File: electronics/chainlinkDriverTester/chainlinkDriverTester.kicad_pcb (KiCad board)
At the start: 2 copper layers, 198.1 x 95.2 mm, 151 parts, among them J1 Barrel_Jack_Switch, J10 Sensor C, J11 Sensor D, J12 Motor E, J13 Motor F, J14 Sensor E, J15 Sensor F, J2 Conn_01x03_Female, J22 Power, J26 exp, J27 exp, J28 exp, J29 exp, J3 Motor A, J30 exp, J31 exp, J32 Conn_01x06_Female, J5 Motor B, J6 Motor C, J7 Motor D, J8 Sensor A, J9 Sensor B, U1 AP7361C-33E, U2 TTGO_TDisplay, U3 VN7007ALH, U4 MCP23017_SS, U5 INA219BxD, U6 SN74LV1T34DBV, U7 Buck

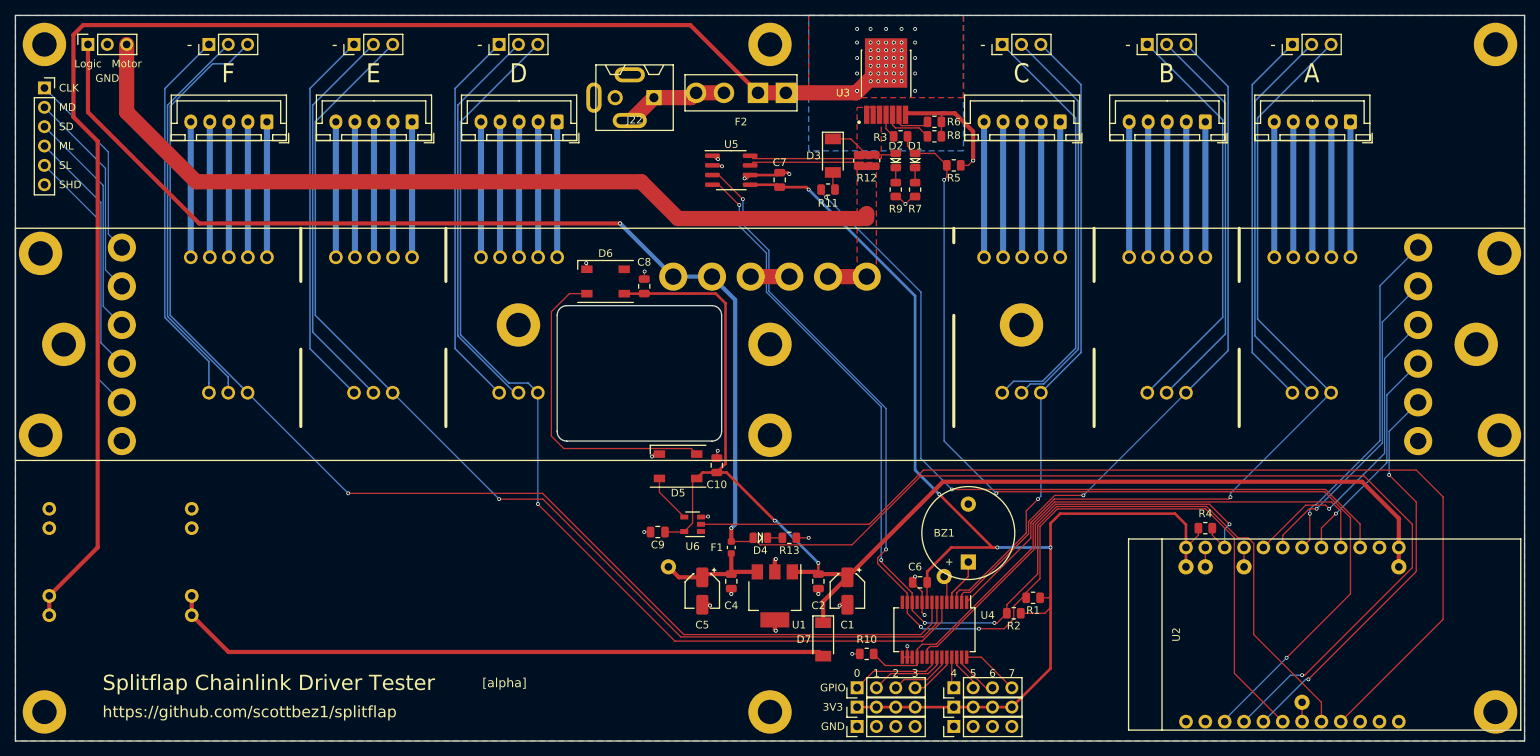
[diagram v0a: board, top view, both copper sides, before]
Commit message: chainlinkDriverTester: remove WS2812B LEDs, add detection switch
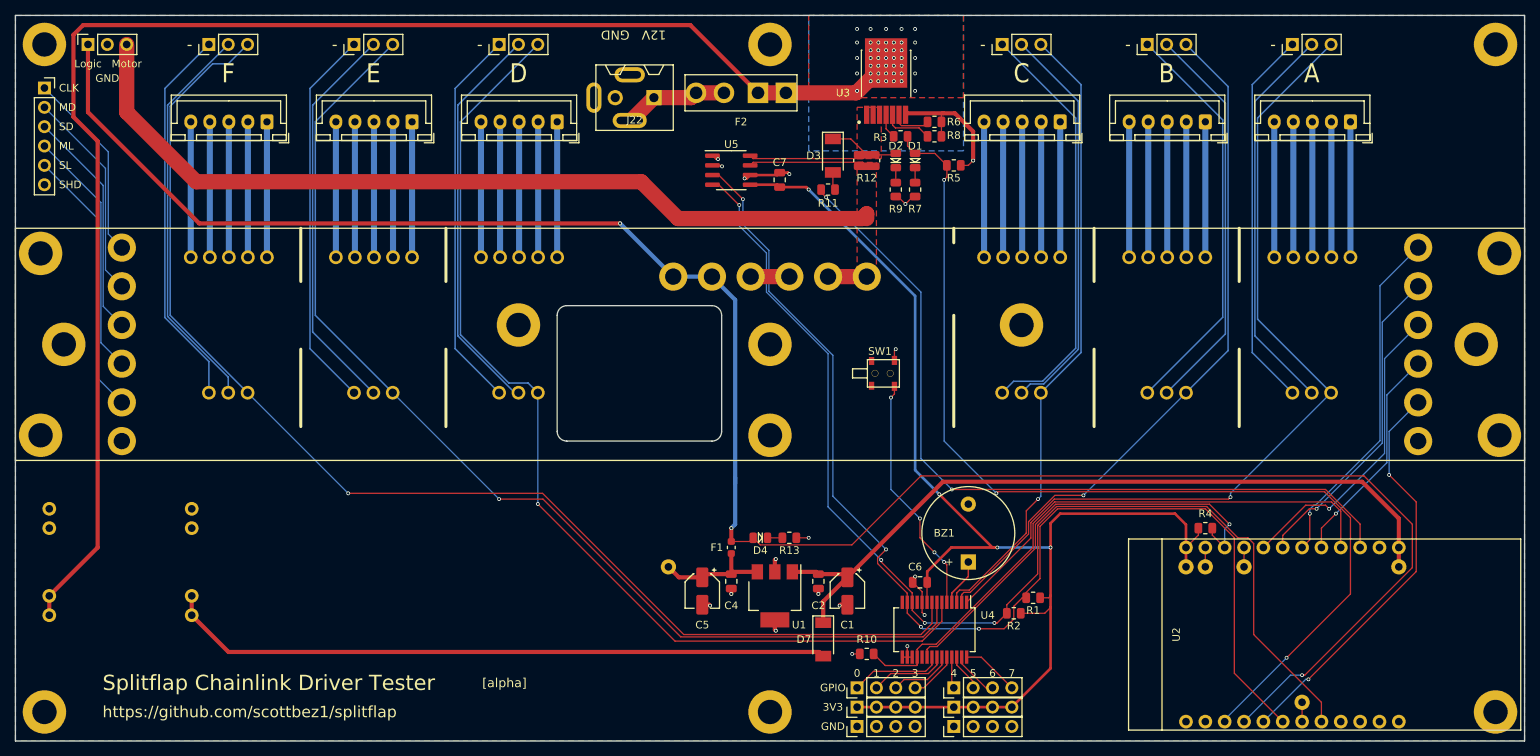
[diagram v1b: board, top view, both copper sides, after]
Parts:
- removed C10, C8, C9: 0.1uF, Capacitor_SMD:C_0805_2012Metric
- removed D5, D6: WS2812B, LED_SMD:LED_WS2812B_PLCC4_5.0x5.0mm_P3.2mm
- removed TP62: TestPoint, TestPoint:TestPoint_THTPad_D2.0mm_Drill1.0mm
- removed U6: SN74LV1T34DBV, Package_TO_SOT_SMD:SOT-23-5
- added SW1: SW_Push, SwitchESE13:ESE13V01D, F.Cu at (137.8, 72.4)
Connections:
- U2 pad 9: /LED -> (no net)
- U4 pad 5: Net-(TP62-Pad1) -> /DETECT
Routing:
- net /LED: track 136.9 -> 0.00 mm
- net +5V: track 170.1 -> 100.7 mm, vias 2 -> 0
- net Net-(D5-Pad2): track 42.0 -> 0.00 mm
- net /DETECT: track 0.00 -> 31.6 mm, vias 0 -> 4
- net Net-(D5-Pad4): track 6.42 -> 0.00 mm
- net GND: track 59.4 -> 55.2 mm, vias 23 -> 18
- net Net-(TP62-Pad1): track 3.53 -> 0.00 mm
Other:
- board text added: "12V"

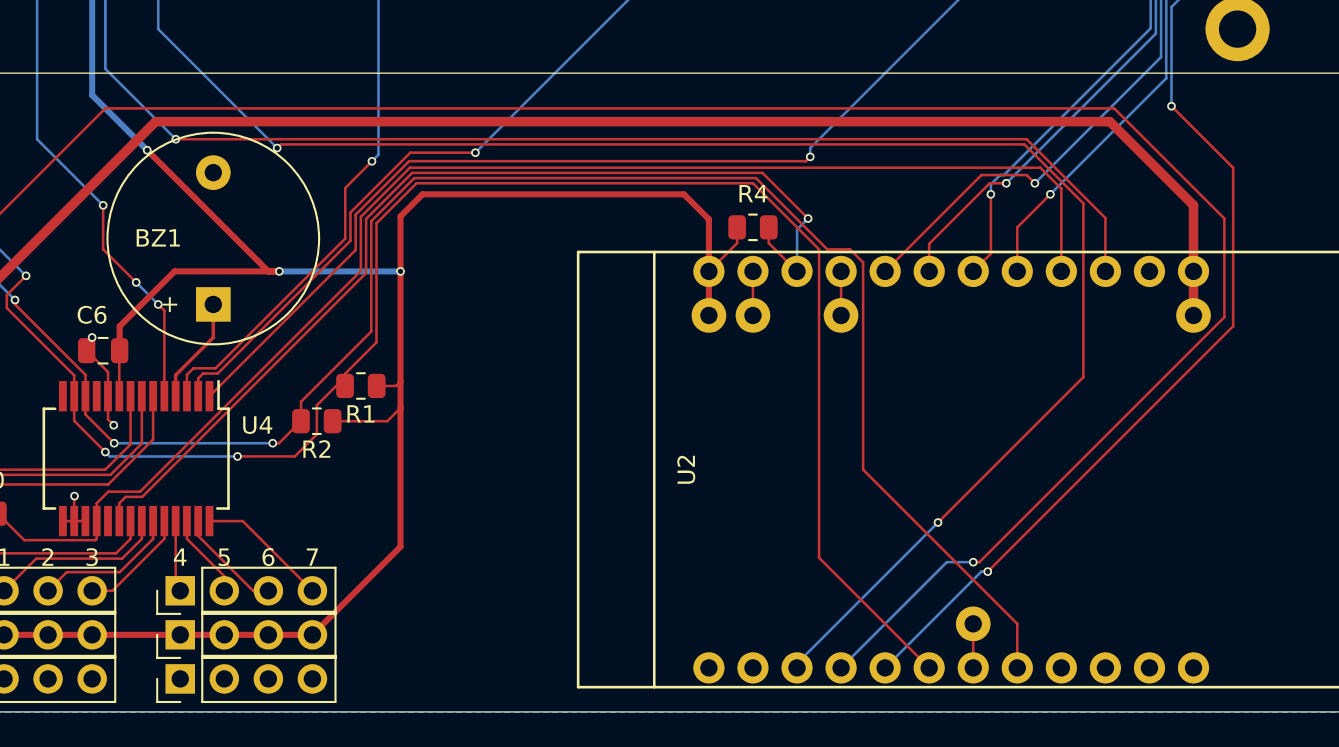
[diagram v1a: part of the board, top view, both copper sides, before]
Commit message: Update chainlink driver tester PCB to match schematic with updated T-Display pinout, add extra row of holes for each pin for convenience
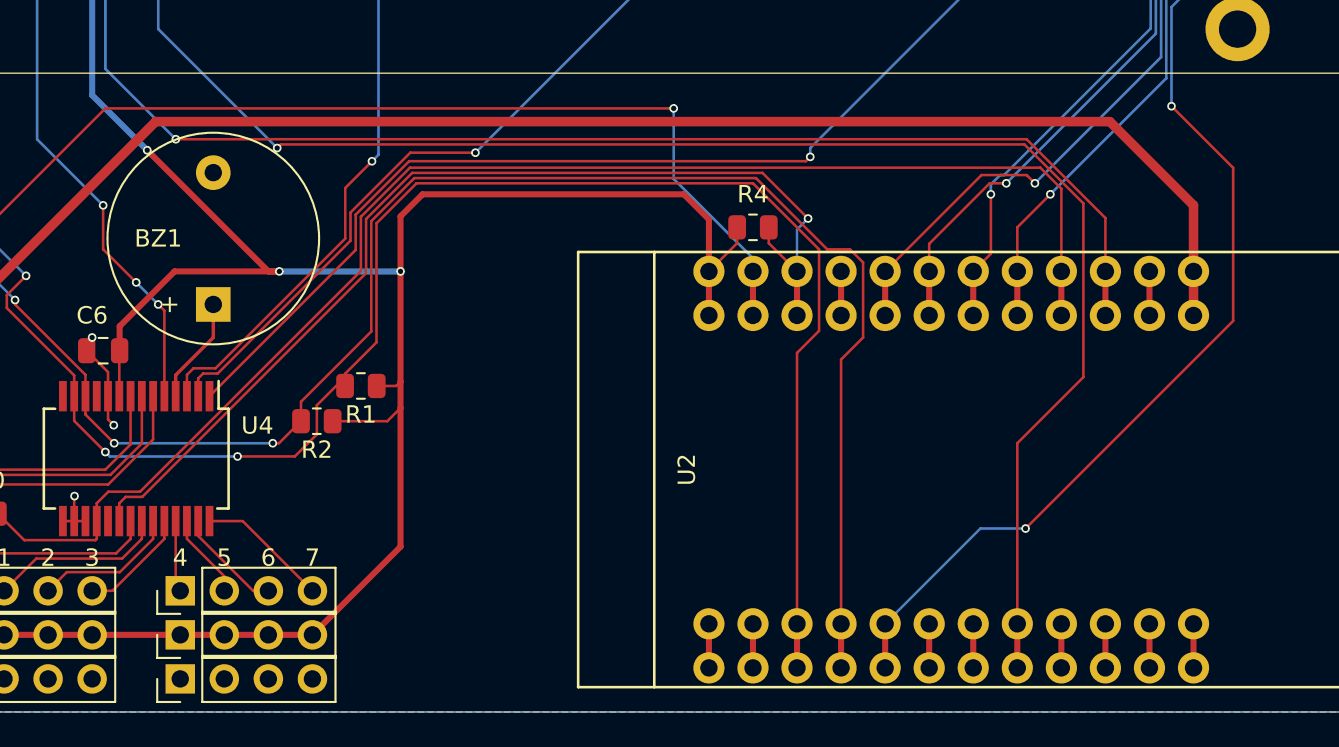
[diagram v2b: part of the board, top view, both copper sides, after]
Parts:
- removed TP69, TP70, TP71, TP73, TP75: TestPoint, TestPoint:TestPoint_THTPad_D2.0mm_Drill1.0mm
- U2: footprint ESP32:T-DISPLAY -> ESP32:T-DISPLAY_extra_pins
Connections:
- U2 pad 12: (no net) -> Net-(U2-Pad12)
- U2 pad 23: Net-(TP69-Pad1) -> /3V3_FUSED
- U2 pad 3: /12V_EN -> /SDA
- U2 pad 4: /3V3_FUSED -> /SCL
- U2 pad 6: /SDA -> Net-(U2-Pad6)
- U2 pad 8: /SCL -> /12V_EN
- U2 pad 9: (no net) -> Net-(U2-Pad9)
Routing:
- net /3V3_FUSED: track 269.3 -> 212.6 mm
- net GND: track 55.2 -> 67.9 mm
- net /12V_EN: track 135.1 -> 132.4 mm, vias 3 -> 2
- net Net-(U2-Pad9): track 0.00 -> 2.54 mm
- net Net-(U2-Pad6): track 0.00 -> 2.54 mm
- net Net-(U2-Pad12): track 0.00 -> 2.54 mm
- net Net-(TP69-Pad1): track 2.54 -> 0.00 mm
- net /SENSOR_DATA: track 40.1 -> 42.6 mm
- net /MOTOR_LATCH: track 29.4 -> 31.9 mm
- net /MOTOR_DATA: track 42.2 -> 44.8 mm
- net /MCP_RESET: track 79.1 -> 81.7 mm
- net /MCP_INT: track 58.1 -> 60.6 mm
- net /CLOCK: track 45.8 -> 48.4 mm
- net /12V_TEST_FEED: track 105.0 -> 107.6 mm
- net /SENSOR_LATCH: track 53.5 -> 54.8 mm
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
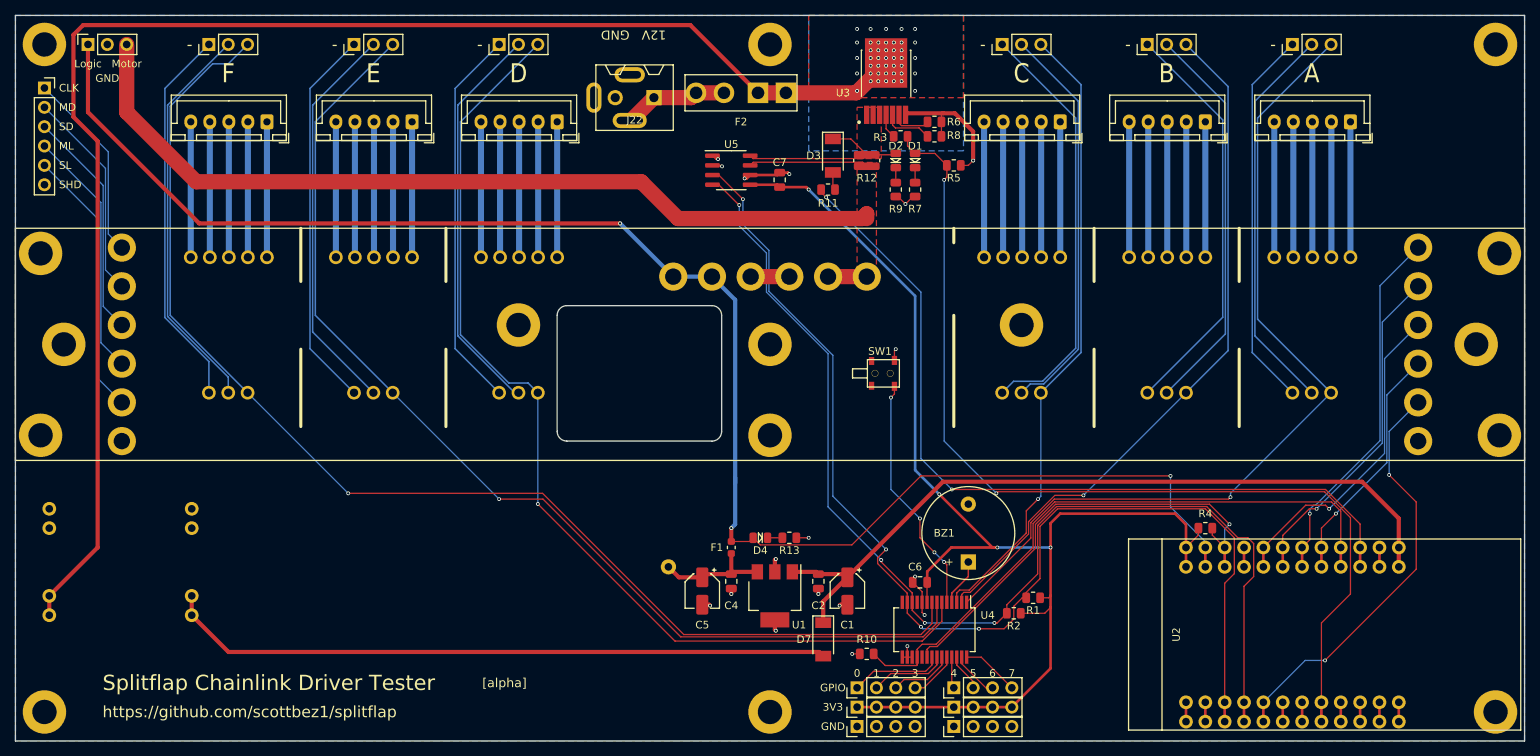
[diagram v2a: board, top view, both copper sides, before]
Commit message: Change Chainlink data connections from screw terminals to IDC (#189)
- Replace screw terminals with 2x4 IDC connectors (alternating ground) on Driver, Base, and Tester. Fixes #179
- Change Chainlink Driver Tester to all 1mm pogo pins
- Create new "Buddy" boards for connecting IDC/ribbon cable to T-Display or a breadboard
- Big readme cleanup and reorganization for clarity (hopefully!)
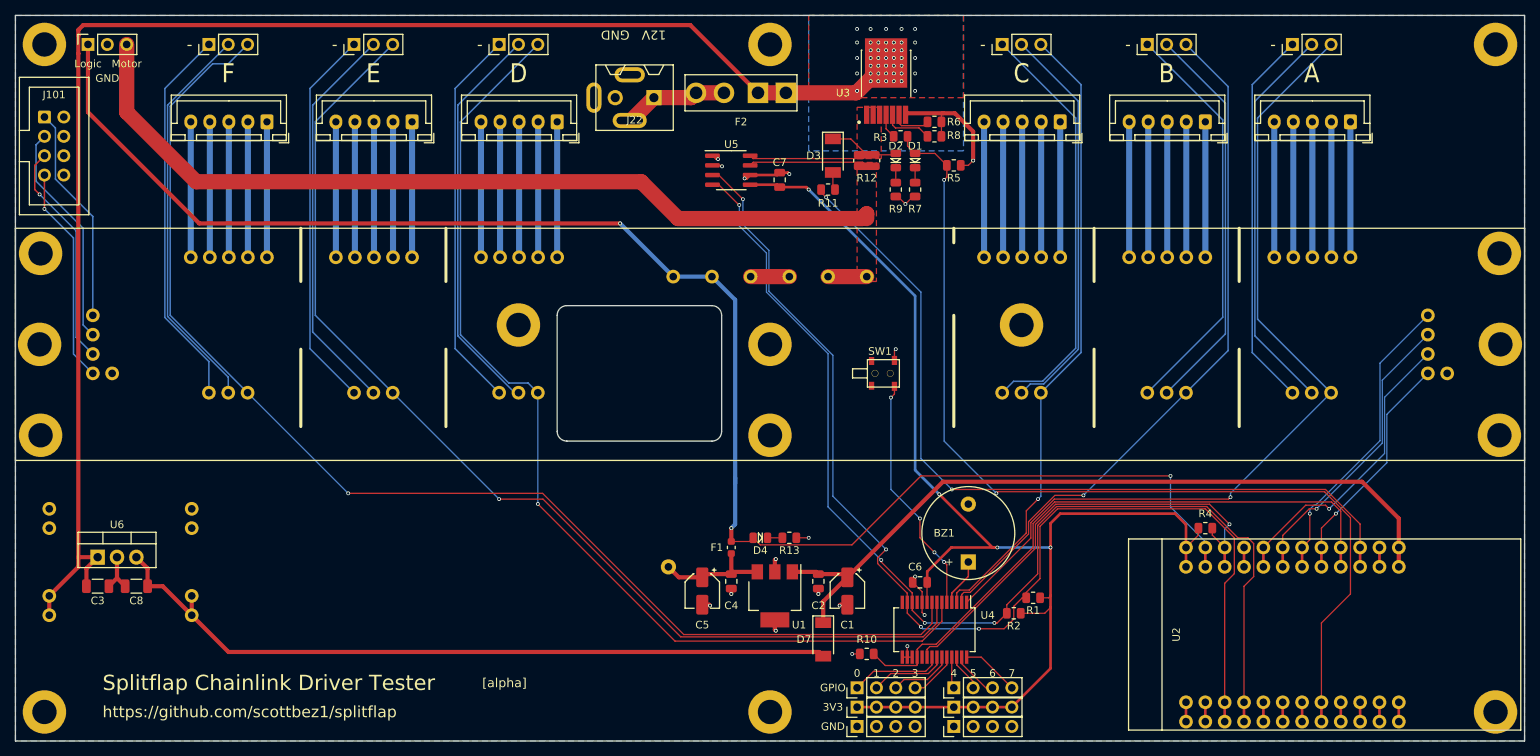
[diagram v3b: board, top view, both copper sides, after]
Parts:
- removed J32: Conn_01x06_Female, Connector_PinSocket_2.54mm:PinSocket_1x06_P2.54mm_Vertical
- removed TP57, TP58: TestPoint, pogoPins:pogo2mm
- added C3: 10uF, Capacitor_SMD:C_1206_3216Metric, F.Cu at (36.2, 100.3)
- added C8: 22uF, Capacitor_SMD:C_1206_3216Metric, F.Cu at (41.3, 100.3)
- added J101: Conn_02x04_Odd_Even, ModifiedSymbols:IDC-Header_2x04_P2.54mm_Vertical, F.Cu at (29.2, 38.7)
- added U6: LM7805_TO220, Package_TO_SOT_THT:TO-220-3_Vertical, F.Cu at (36.2, 96.5)
- TP49, TP50, TP51, TP52, TP53, TP54, TP55, TP56, TP59, TP60, TP63, TP64, TP65, TP66, TP67, TP68: footprint pogoPins:pogo2mm -> pogoPins:pogo1mm
- moved TP59 9.67 mm to (213.4, 72.4)
- moved TP50 9.67 mm to (35.6, 64.8)
- moved TP60 8.98 mm to (38.1, 72.4)
- moved TP49 8.98 mm to (210.8, 64.8)
- moved TP52 7.41 mm to (35.6, 67.3)
- moved TP51 6.48 mm to (210.8, 67.3)
- moved TP54 5.39 mm to (35.6, 69.8)
- moved TP56 4.02 mm to (35.6, 72.4)
- moved TP53 4.02 mm to (210.8, 69.8)
- moved H14 3.18 mm to (220.3, 68.6)
- moved H10 3.18 mm to (28.6, 68.6)
- moved TP55 1.80 mm to (210.8, 72.4)
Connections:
- net /MOTOR_LATCH renamed /LATCH
- TP56 pad 1: /MOTOR_LATCH_OUT -> /LATCH_OUT
- U2 pad 5: /SENSOR_LATCH -> Net-(U2-Pad5)
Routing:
- net /SENSOR_LATCH: track 54.8 -> 0.00 mm, vias 2 -> 0
- net /SENSOR_LATCH_OUT: track 35.3 -> 0.00 mm
- net /MOTOR_LATCH_OUT: track 33.4 -> 0.00 mm
- net /LATCH_OUT: track 0.00 -> 28.7 mm, vias 0 -> 1
- net Net-(C8-Pad1): track 87.7 -> 99.5 mm
- net /CLOCK: track 48.4 -> 40.0 mm
- net /MOTOR_DATA: track 44.8 -> 38.9 mm
- net GND: track 67.9 -> 73.6 mm
- net /SW_IN: track 192.7 -> 197.0 mm
- net /CLOCK_OUT: track 25.2 -> 28.7 mm
- net /SENSOR_DATA: track 42.6 -> 39.4 mm
- net Net-(U2-Pad5): track 0.00 -> 2.54 mm
- net /MOTOR_OUT: track 27.7 -> 29.6 mm
- net /LATCH: track 31.9 -> 31.2 mm
- net /SENSOR_IN: track 30.2 -> 29.7 mm, vias 0 -> 1
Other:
- board text removed: "CLK"
- board text removed: "MD"
- board text removed: "ML"
- board text removed: "SD"
- board text removed: "SHD"
- board text removed: "SL"

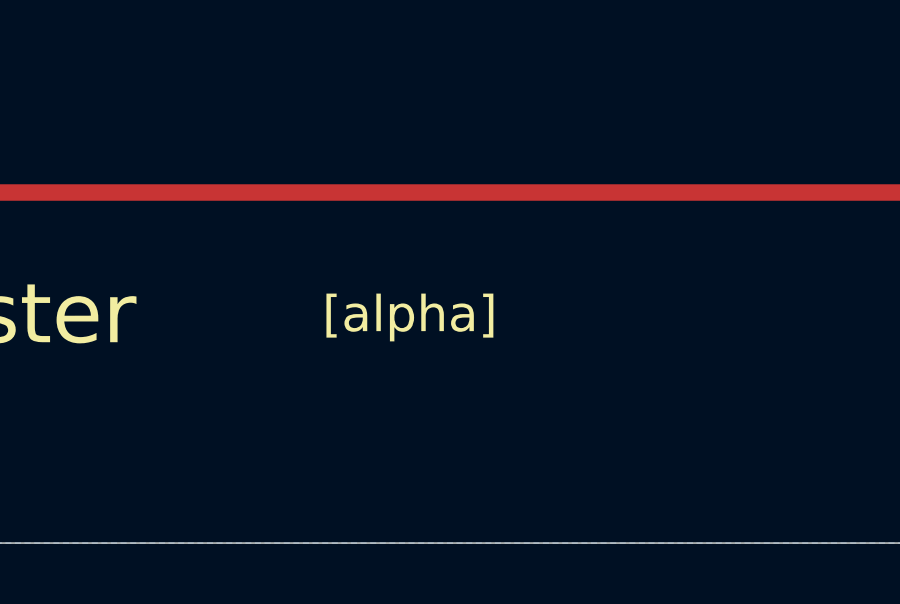
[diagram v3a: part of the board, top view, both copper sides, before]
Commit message: Add version numbers to chainlink PCBs
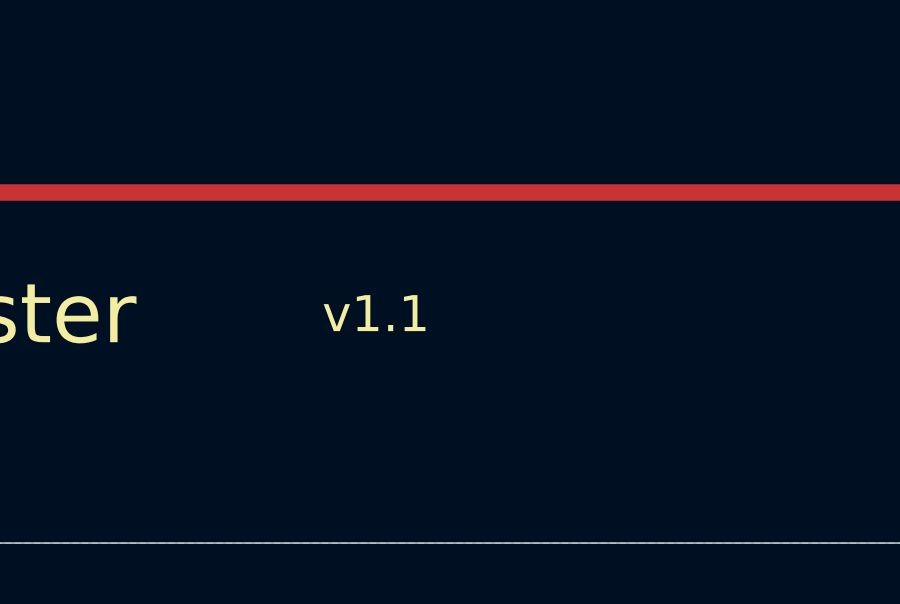
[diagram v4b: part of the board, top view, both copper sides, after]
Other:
- board text added: "v1.1"
- board text removed: "[alpha]"
